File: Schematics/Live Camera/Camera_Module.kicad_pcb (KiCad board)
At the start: 4 copper layers, 69.5 x 56 mm, 2 parts, among them J1 Stack Male Edge Connector, J3 SWD_01x04_Pin

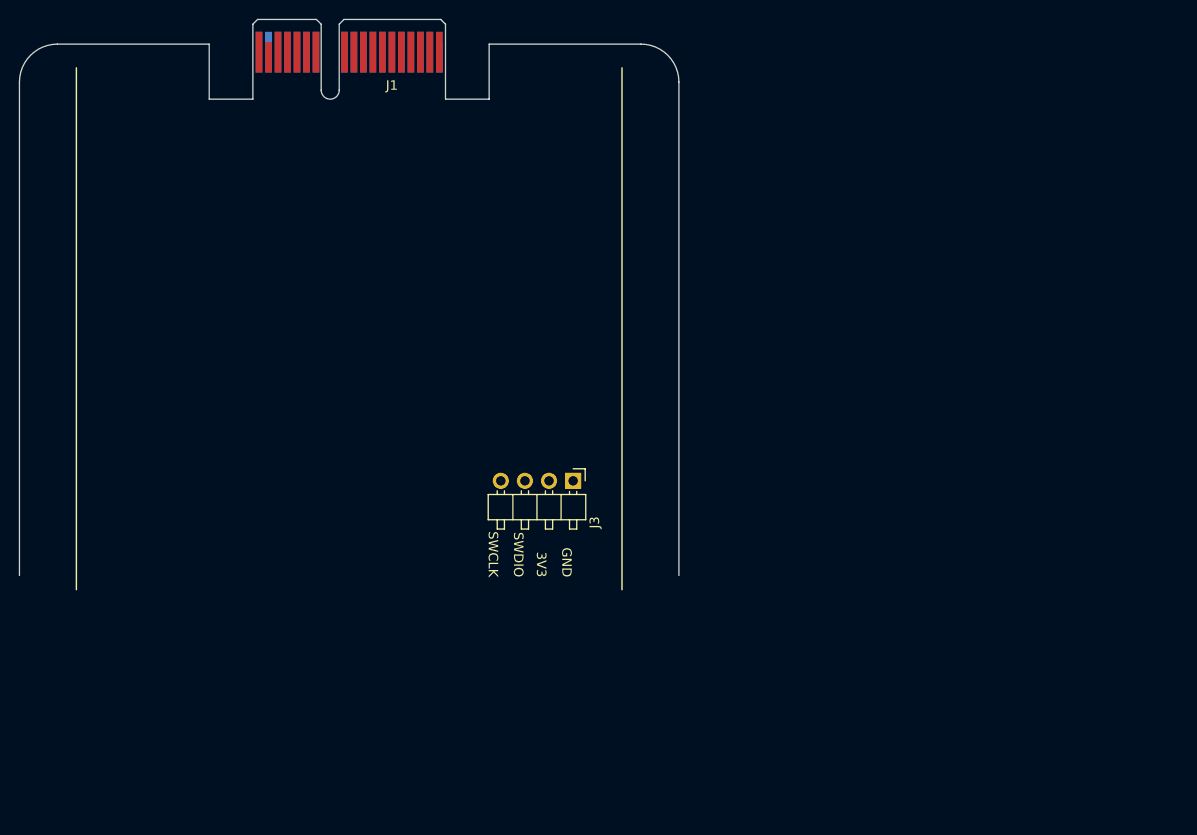
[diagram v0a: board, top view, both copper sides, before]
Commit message: Added Camera Module Layout
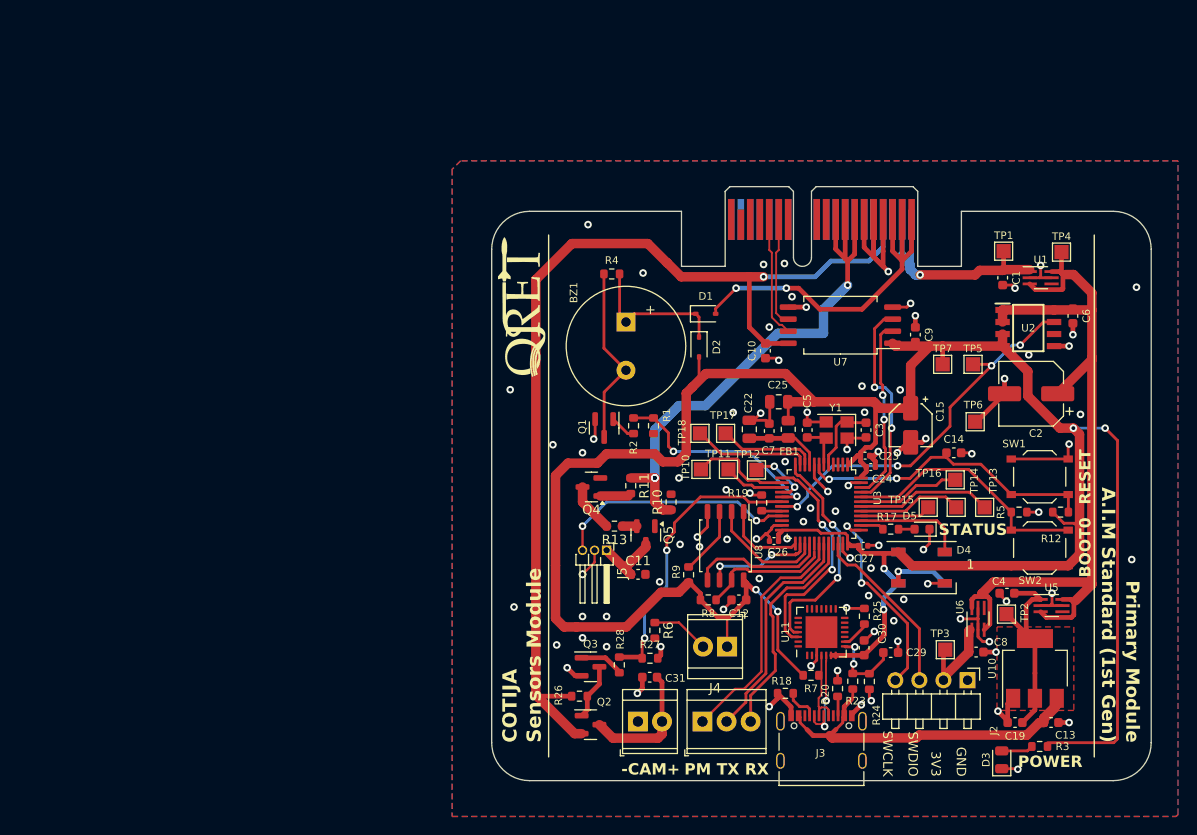
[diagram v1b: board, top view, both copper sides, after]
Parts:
- added BZ1: PKM13EPYH4000, footprints:Buzzer_12.6x9.5RM5.0, F.Cu at (101.1, 58.5)
- added C1: 1uF, Capacitor_SMD:C_0603_1608Metric, F.Cu at (140.8, 55.1)
- added C10: 0.1u, Capacitor_SMD:C_0603_1608Metric, F.Cu at (115.8, 62.8)
- added C11: 10uF, Capacitor_SMD:C_0603_1608Metric, F.Cu at (102.4, 86.4)
- added C12: 100nF, Capacitor_SMD:C_0603_1608Metric, F.Cu at (113.0, 89.0)
- added C13: 10uF, Capacitor_SMD:C_0603_1608Metric, F.Cu at (145.9, 102.0)
- added C14: 100nF, Capacitor_SMD:C_0603_1608Metric, F.Cu at (135.7, 73.5)
- added C15: 10uF, Capacitor_SMD:CP_Elec_4x5.4, F.Cu at (131.1, 70.7)
- added C19: 10uF, Capacitor_SMD:C_0603_1608Metric, F.Cu at (142.1, 102.0)
- added C2: 100uF, Capacitor_SMD:CP_Elec_6.3x5.9, F.Cu at (143.8, 67.3)
- added C22: 1uF, Capacitor_SMD:C_0805_2012Metric, F.Cu at (114.1, 71.1)
- added C23: 100n, Capacitor_SMD:C_0402_1005Metric, F.Cu at (126.3, 73.8)
- added C24: 100n, Capacitor_SMD:C_0402_1005Metric, F.Cu at (126.9, 75.0)
- added C25: 1uF, Capacitor_SMD:C_0805_2012Metric, F.Cu at (117.2, 68.2)
- added C26: 100n, Capacitor_SMD:C_0402_1005Metric, F.Cu at (116.7, 82.8)
- added C27: 100n, Capacitor_SMD:C_0402_1005Metric, F.Cu at (126.1, 83.3)
- added C29: 1uF, Capacitor_SMD:C_0603_1608Metric, F.Cu at (129.0, 94.6)
- added C3: 10p, Capacitor_SMD:C_0603_1608Metric, F.Cu at (126.4, 71.2)
- added C30: 10uF, Capacitor_SMD:C_0603_1608Metric, F.Cu at (126.2, 94.1)
- added C31: 10uF, Capacitor_SMD:C_0603_1608Metric, F.Cu at (103.6, 97.2)
- added C4: 1uF, Capacitor_SMD:C_0603_1608Metric, F.Cu at (141.2, 88.3)
- added C5: 10p, Capacitor_SMD:C_0603_1608Metric, F.Cu at (120.2, 71.2)
- added C6: 0.1uF, Capacitor_SMD:C_0603_1608Metric, F.Cu at (148.2, 59.1)
- added C7: 10n, Capacitor_SMD:C_0603_1608Metric, F.Cu at (116.2, 71.2)
- added C8: 1uF, Capacitor_SMD:C_0603_1608Metric, F.Cu at (138.0, 94.5)
- added C9: 0.1u, Capacitor_SMD:C_0603_1608Metric, F.Cu at (131.6, 61.1)
- added D1: 1N5819WS, Diode_SMD:D_SOD-323, F.Cu at (109.5, 58.9)
- added D2: 1N5819WS, Diode_SMD:D_SOD-323, F.Cu at (108.8, 62.4)
- added D3: PWR_LED (GRN), LED_SMD:LED_0805_2012Metric, F.Cu at (140.7, 105.9)
- added D4: WS2812B, LED_SMD:LED_WS2812B_PLCC4_5.0x5.0mm_P3.2mm, F.Cu at (132.2, 85.7)
- added D5: DB_LED (YLW), LED_SMD:LED_0603_1608Metric, F.Cu at (132.3, 81.6)
- added D6: WS2812B, LED_SMD:LED_WS2812B_PLCC4_5.0x5.0mm_P3.2mm, B.Cu at (132.2, 85.7)
- added FB1: 100R, Resistor_SMD:R_0805_2012Metric, F.Cu at (118.2, 71.1)
- added J2: SWD_01x04_Pin, SWD_Header:SWD_PinHeader_1x04_P2.54mm_Horizontal, F.Cu at (137.1, 97.5)
- added J4: Screw_Terminal_01x02, TerminalBlock_TE-Connectivity:TerminalBlock_TE_282834-2_1x02_P2.54mm_Horizontal, F.Cu at (111.8, 94.0)
- added J5: Conn_01x03_Pin, Connector_PinHeader_1.27mm:PinHeader_1x03_P1.27mm_Horizontal, F.Cu at (99.1, 83.8)
- added J6: CAM_PWR, TerminalBlock_TE-Connectivity:TerminalBlock_TE_282834-2_1x02_P2.54mm_Horizontal, F.Cu at (102.4, 101.9)
- added J7: CAM_DAT, TerminalBlock_TE-Connectivity:TerminalBlock_TE_282834-3_1x03_P2.54mm_Horizontal, F.Cu at (109.2, 101.9)
- added Q1: AO3400A, Package_TO_SOT_SMD:SOT-23, F.Cu at (98.8, 70.9)
- added Q2: AO3401A, Package_TO_SOT_SMD:SOT-23, F.Cu at (97.4, 102.2)
- added Q3: AO3400A, Package_TO_SOT_SMD:SOT-23, F.Cu at (97.4, 96.1)
- added Q4: AO3400A, Package_TO_SOT_SMD:SOT-23, F.Cu at (97.5, 77.2)
- added Q5: AO3401A, Package_TO_SOT_SMD:SOT-23, F.Cu at (103.2, 82.2)
- added R1: 10k, Resistor_SMD:R_0603_1608Metric, F.Cu at (104.0, 70.7)
- added R10: 100k, Resistor_SMD:R_0603_1608Metric, F.Cu at (105.9, 78.7)
- added R11: 820, Resistor_SMD:R_0603_1608Metric, F.Cu at (101.6, 77.0)
- added R12: 10k, Resistor_SMD:R_0603_1608Metric, F.Cu at (146.9, 79.8)
- added R13: 100k, Resistor_SMD:R_0603_1608Metric, F.Cu at (99.9, 81.3)
- added R17: 680R, Resistor_SMD:R_0603_1608Metric, F.Cu at (129.0, 81.6)
- added R18: 5.1k, Resistor_SMD:R_0603_1608Metric, F.Cu at (117.9, 98.9)
- added R19: 100k, Resistor_SMD:R_0603_1608Metric, F.Cu at (115.4, 78.8)
- added R2: 510R, Resistor_SMD:R_0603_1608Metric, F.Cu at (101.9, 70.7)
- added R20: 5.1k, Resistor_SMD:R_0603_1608Metric, F.Cu at (123.4, 98.4)
- added R23: 22k, Resistor_SMD:R_0603_1608Metric, F.Cu at (125.0, 97.6)
- added R24: 47k, Resistor_SMD:R_0603_1608Metric, F.Cu at (126.8, 97.7)
- added R25: 1k, Resistor_SMD:R_0603_1608Metric, F.Cu at (126.2, 90.8)
- added R26: 100k, Resistor_SMD:R_0603_1608Metric, F.Cu at (96.2, 99.2)
- added R27: 100k, Resistor_SMD:R_0603_1608Metric, F.Cu at (103.6, 95.2)
- added R28: 510, Resistor_SMD:R_0603_1608Metric, F.Cu at (100.4, 95.9)
- added R3: 3.3k, Resistor_SMD:R_0603_1608Metric, F.Cu at (144.7, 104.5)
- added R4: 1k, Resistor_SMD:R_0603_1608Metric, F.Cu at (99.6, 54.7)
- added R5: 100k, Resistor_SMD:R_0603_1608Metric, F.Cu at (142.5, 79.8)
- added R6: 10k, Resistor_SMD:R_0603_1608Metric, F.Cu at (104.1, 92.3)
- added R7: 1.5k, Resistor_SMD:R_0603_1608Metric, F.Cu at (120.6, 97.0)
- added R8: 10k, Resistor_SMD:R_0603_1608Metric, F.Cu at (109.8, 89.0)
- added R9: 10k, Resistor_SMD:R_0603_1608Metric, F.Cu at (107.7, 86.4)
- added SW1: SW_STM_RESET, Button_Switch_SMD:SW_Push_1P1T_XKB_TS-1187A, F.Cu at (144.7, 76.1)
- added SW2: SW_STM_BOOT_MODE, Button_Switch_SMD:SW_Push_1P1T_XKB_TS-1187A, F.Cu at (144.7, 83.6)
- added TP1: TP_VSTACK, TestPoint:TestPoint_Pad_1.5x1.5mm, F.Cu at (140.9, 52.3)
- added TP10: PA4, TestPoint:TestPoint_Pad_1.5x1.5mm, F.Cu at (109.0, 75.3)
- added TP11: PA5, TestPoint:TestPoint_Pad_1.5x1.5mm, F.Cu at (111.9, 75.3)
- added TP12: PA6, TestPoint:TestPoint_Pad_1.5x1.5mm, F.Cu at (114.8, 75.3)
- added TP13: PB6, TestPoint:TestPoint_Pad_1.5x1.5mm, F.Cu at (138.9, 79.3)
- added TP14: PB5, TestPoint:TestPoint_Pad_1.5x1.5mm, F.Cu at (135.9, 79.3)
- added TP15: PB4, TestPoint:TestPoint_Pad_1.5x1.5mm, F.Cu at (132.9, 79.3)
- added TP16: PB7, TestPoint:TestPoint_Pad_1.5x1.5mm, F.Cu at (135.8, 76.4)
- added TP17: PA0, TestPoint:TestPoint_Pad_1.5x1.5mm, F.Cu at (111.6, 71.5)
- added TP18: PA1, TestPoint:TestPoint_Pad_1.5x1.5mm, F.Cu at (108.9, 71.5)
- added TP2: TP_VUSB, TestPoint:TestPoint_Pad_1.5x1.5mm, F.Cu at (141.2, 90.5)
- added TP3: TP_VSWD, TestPoint:TestPoint_Pad_1.5x1.5mm, F.Cu at (134.8, 94.3)
- added TP4: TP_MUX, TestPoint:TestPoint_Pad_1.5x1.5mm, F.Cu at (147.0, 52.4)
- added TP5: TP_ISENSE, TestPoint:TestPoint_Pad_1.5x1.5mm, F.Cu at (137.7, 64.2)
- added TP6: TP_GND, TestPoint:TestPoint_Pad_1.5x1.5mm, F.Cu at (137.9, 70.3)
- added TP7: TP_3V3, TestPoint:TestPoint_Pad_1.5x1.5mm, F.Cu at (134.5, 64.2)
- added U1: LM66100DCKR, LMR66100:SC-70-6_Handsoldering, F.Cu at (144.8, 55.1)
- added U10: AMS1117-3.3, Package_TO_SOT_SMD:SOT-223-3_TabPin2, F.Cu at (144.2, 96.3)
- added U11: CP2102N-Axx-xQFN28, Package_DFN_QFN:QFN-28-1EP_5x5mm_P0.5mm_EP3.35x3.35mm, F.Cu at (121.7, 92.5)
- added U2: ACS70331EOLC, footprints:SOIC127P600X175-8N, F.Cu at (143.5, 60.4)
- added U3: STM32F103CBT6, Package_QFP:LQFP-48_7x7mm_P0.5mm, F.Cu at (121.7, 79.0)
- added U5: LM66100DCKR, LMR66100:SC-70-6_Handsoldering, F.Cu at (145.9, 89.7)
- added U6: LM66100DCKR, LMR66100:SC-70-6_Handsoldering, F.Cu at (138.2, 91.0)
- added U7: ISO1042BDWVR, ISO1042:SOIC-8 ISO1042BDWV, F.Cu at (123.7, 60.1)
- added U8: W25Q128JVS, Package_SO:SOIC-8_5.23x5.23mm_P1.27mm, F.Cu at (111.6, 83.3)
- added Y1: X322516MMB4SI, Crystal:Crystal_SMD_3225-4Pin_3.2x2.5mm, F.Cu at (123.3, 71.2)
- J3: value SWD_01x04_Pin -> USB_C_Female_USB2_Small; footprint SWD_Header:SWD_PinHeader_1x04_P2.54mm_Horizontal -> footprints:USB_C_DB-108PWB
- moved J1 52.8 mm to (131.2, 49.0)
- moved J3 37.8 mm to (121.7, 103.8), turned to 0 degrees
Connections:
- J1 pad A1: (no net) -> V_PSU
- J1 pad A10: (no net) -> unconnected-(J1-Reserved-PadA10)
- J1 pad A11: (no net) -> unconnected-(J1-Reserved-PadA11)
- J1 pad A12: (no net) -> GND
- J1 pad A13: (no net) -> unconnected-(J1-DB_LED-PadA13)
- J1 pad A14: (no net) -> unconnected-(J1-Reserved-PadA14)
- J1 pad A15: (no net) -> unconnected-(J1-Reserved-PadA15)
- J1 pad A16: (no net) -> unconnected-(J1-Reserved-PadA16)
- J1 pad A17: (no net) -> unconnected-(J1-Reserved-PadA17)
- J1 pad A18: (no net) -> unconnected-(J1-Reserved-PadA18)
- J1 pad A2: (no net) -> V_PSU
- J1 pad A3: (no net) -> GND
- J1 pad A4: (no net) -> +5V
- J1 pad A5: (no net) -> +5V
- J1 pad A6: (no net) -> GND
- J1 pad A7: (no net) -> unconnected-(J1-3.3V_B-PadA7)_1
- J1 pad A8: (no net) -> unconnected-(J1-3.3V_B-PadA7)
- J1 pad A9: (no net) -> GND
- J1 pad B1: (no net) -> +BATT
- J1 pad B10: (no net) -> GND
- J1 pad B11: (no net) -> GND
- J1 pad B12: (no net) -> GND
- J1 pad B13: (no net) -> CAN_L
- J1 pad B14: (no net) -> CAN_H
- J1 pad B15: (no net) -> unconnected-(J1-Reserved-PadB15)
- J1 pad B16: (no net) -> unconnected-(J1-Reserved-PadB16)
- J1 pad B17: (no net) -> unconnected-(J1-Reserved-PadB17)
- J1 pad B18: (no net) -> unconnected-(J1-Reserved-PadB18)
- J1 pad B2: (no net) -> +BATT
- J1 pad B3: (no net) -> +BATT
- J1 pad B4: (no net) -> GND
- J1 pad B5: (no net) -> GND
- J1 pad B6: (no net) -> GND
- J1 pad B7: (no net) -> VTX_PWR
- J1 pad B8: (no net) -> VTX_PWR
- J1 pad B9: (no net) -> VTX_PWR
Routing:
- net +3.3V: track 0.00 -> 273.8 mm, vias 0 -> 6
- net GND: track 0.00 -> 135.8 mm, vias 0 -> 90
- net +5V: track 0.00 -> 111.7 mm, vias 0 -> 1
- net V_MUX: track 0.00 -> 87.1 mm
- net VTX_PWR: track 0.00 -> 57.0 mm, vias 0 -> 4
- net CURR_SENSE: track 0.00 -> 40.3 mm, vias 0 -> 4
- net 5V_RAW: track 0.00 -> 39.9 mm
- net +BATT: track 0.00 -> 38.5 mm, vias 0 -> 2
- net STM_RESET: track 0.00 -> 32.3 mm, vias 0 -> 2
- net CAM_PWR: track 0.00 -> 30.8 mm, vias 0 -> 2
- net BOOT0: track 0.00 -> 26.8 mm
- net CAM_TX: track 0.00 -> 25.6 mm
- net VTX_DATA: track 0.00 -> 25.6 mm, vias 0 -> 2
- net V_PSU: track 0.00 -> 25.0 mm, vias 0 -> 1
- net CAM_RX: track 0.00 -> 24.2 mm
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- added copper zone on B.Cu, net GND
- added copper zone on F.Cu, net GND
- added copper zone on F.Cu, net V_REGUSB
- removed copper zone on In1.Cu, net (none)
- removed copper zone on In2.Cu, net (none)
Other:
- board size 69.5 x 56 mm -> 69.5 x 60 mm
- copper layers 4 -> 2
- board text added: "-CAM+"
- board text added: "A.I.M Standard (1st Gen)"
- board text added: "BOOT0"
- board text added: "COTIJA"
- board text added: "Cotija Rev 1.0A QRET May 2024 Ethan Toste Kennan Bays"
- board text added: "JLCJLCJLCJLC"
- board text added: "PM TX RX"
- board text added: "POWER"
- board text added: "Primary Module"
- board text added: "RESET"
- board text added: "STATUS"
- board text added: "Sensors Module"

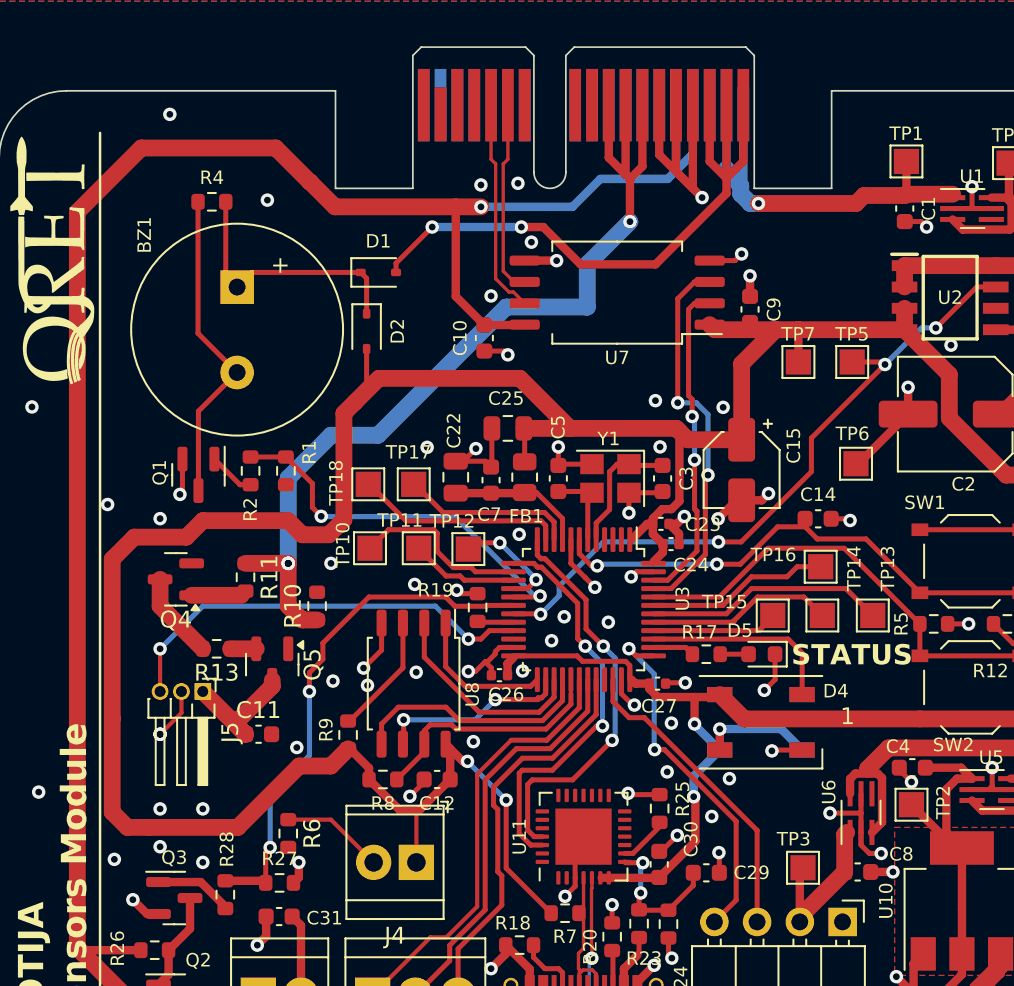
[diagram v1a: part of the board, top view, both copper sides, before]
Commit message: Updated the Camera Module
-connect the thermistor vdiv (V_THERM) to the microcontroller (analog pin)
-add the correct battery connector for the VTX battery (Mate-n-lok, same as on power module / altimeter)
- plus an extra connector for the screw switch,
-connect the VTX control mosfet to the microcontroller
- change the CP2102's reset resistor (R25) to be a pull UP rather than a pull DOWN
-replace the 3-pin pin headers with a proper screw terminal.
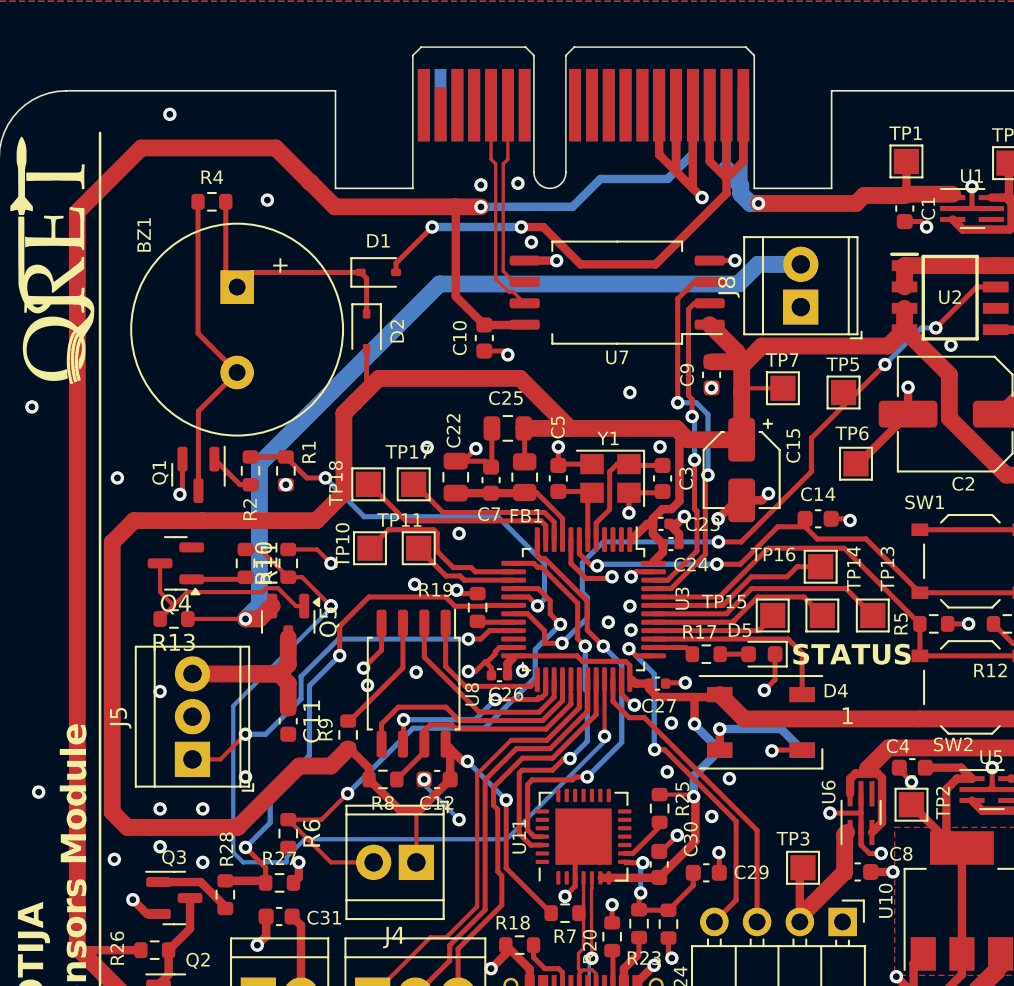
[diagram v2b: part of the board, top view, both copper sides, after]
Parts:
- removed TP12: PA6, TestPoint:TestPoint_Pad_1.5x1.5mm
- added J8: VTX_PWR, TerminalBlock_TE-Connectivity:TerminalBlock_TE_282834-2_1x02_P2.54mm_Horizontal, F.Cu at (134.6, 61.0)
- J5: value Conn_01x03_Pin -> VTX_DAT; footprint Connector_PinHeader_1.27mm:PinHeader_1x03_P1.27mm_Horizontal -> TerminalBlock_TE-Connectivity:TerminalBlock_TE_282834-3_1x03_P2.54mm_Horizontal
- moved C9 4.51 mm to (129.3, 65.0), turned to 90 degrees
- moved J5 4.08 mm to (98.4, 87.9), turned to 90 degrees
- moved R13 3.10 mm to (97.3, 79.5)
- moved R10 3.06 mm to (104.1, 76.2)
- moved Q5 2.71 mm to (104.1, 79.7)
- moved C11 1.93 mm to (104.1, 85.6), turned to -90 degrees
- moved TP5 1.89 mm to (137.2, 66.0)
- moved TP7 1.81 mm to (133.6, 65.8)
- moved Q4 0.95 mm to (97.5, 76.2)
- moved R11 0.83 mm to (101.6, 76.2)
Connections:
- net +8V renamed VTX_8V
- J1 pad A12: GND -> unconnected-(J1-GND_B-PadA12)_1
- J1 pad A9: GND -> unconnected-(J1-GND_B-PadA12)_2
- J1 pad B10: GND -> unconnected-(J1-GND_B-PadA12)
- J1 pad B11: GND -> unconnected-(J1-GND_B-PadA12)_3
- J1 pad B12: GND -> unconnected-(J1-GND_B-PadA12)_4
- J1 pad B7: VTX_PWR -> unconnected-(J1-BATT_B-PadB7)_1
- J1 pad B8: VTX_PWR -> unconnected-(J1-BATT_B-PadB7)_2
- J1 pad B9: VTX_PWR -> unconnected-(J1-BATT_B-PadB7)
- J5 pad 1: VTX_BAT -> VTX_DATA
- J5 pad 3: VTX_DATA -> VTX_BAT
- R25 pad 2: GND -> +3.3V
- U3 pad 16: Net-(U3-PA6) -> V_THERM
- U3 pad 33: unconnected-(U3-PA12-Pad33) -> VTX_PWR
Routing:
- net VTX_8V: track 1.53 -> 52.0 mm, vias 0 -> 1
- net V_THERM: track 6.13 -> 32.2 mm, vias 0 -> 2
- net Net-(Q4-D): track 5.18 -> 12.6 mm
- net Net-(U3-PA6): track 6.69 -> 0.00 mm, vias 2 -> 0
- net VTX_PWR: track 57.0 -> 52.7 mm
- net VTX_BAT: track 7.98 -> 11.8 mm
- net CURR_SENSE: track 40.3 -> 42.9 mm
- net VTX_DATA: track 25.6 -> 23.0 mm
- net +3.3V: track 273.8 -> 276.1 mm
- net BUZZER: track 23.1 -> 24.4 mm
- net GND: track 135.8 -> 134.7 mm, vias 90 -> 85
- net CAM_PWR: track 30.8 -> 31.8 mm
- net USB_RX: track 24.1 -> 23.3 mm
- net USB_TX: track 23.9 -> 24.7 mm

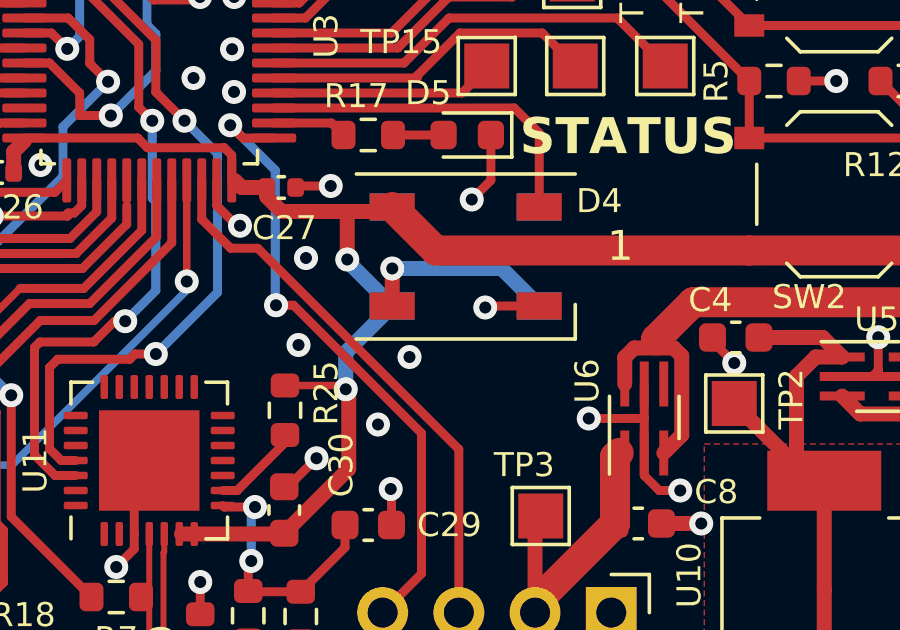
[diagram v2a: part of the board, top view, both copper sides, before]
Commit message: Tweaked attribution silkscreen
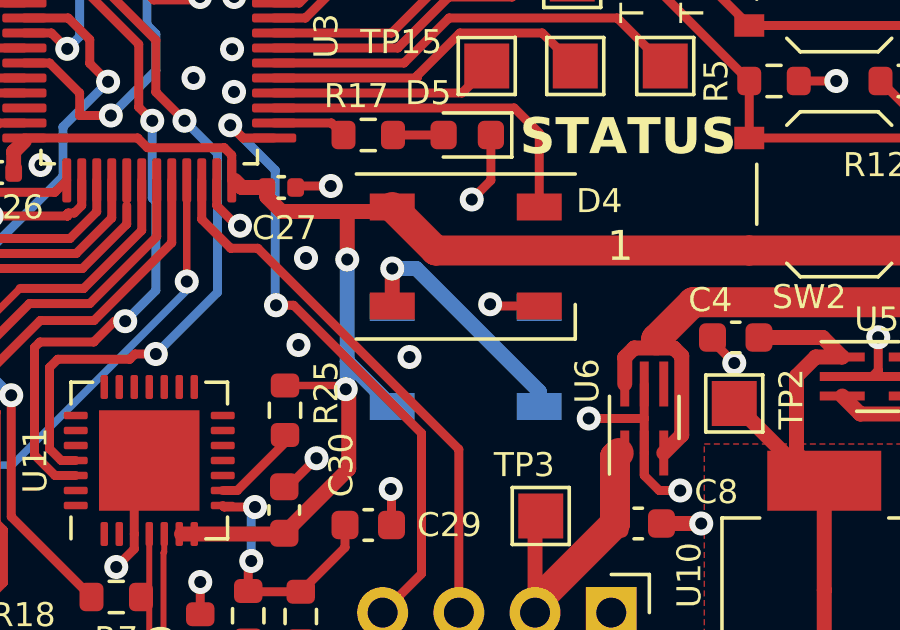
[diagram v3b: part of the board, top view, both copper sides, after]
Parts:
- moved D6 3.35 mm to (132.2, 89.0)
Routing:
- net Net-(D4-DOUT): track 6.67 -> 8.35 mm
- net +3.3V: track 276.1 -> 277.0 mm
- net GND: track 134.7 -> 134.5 mm, vias 85 -> 84
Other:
- board text added: "?????? Rev 1.0 QRET Feb 2025 Ethan Toste Kennan Bays Noah Del Rizzo Fedor Kim"
- board text added: "SET GRID TO MULTIPLE OF 0.1MM (0.1MM, 0.2MM, 0.3MM, ETC)"
- board text removed: "Cotija Rev 1.0A QRET May 2024 Ethan Toste Kennan Bays"
